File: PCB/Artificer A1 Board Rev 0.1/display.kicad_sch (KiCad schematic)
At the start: 2 parts

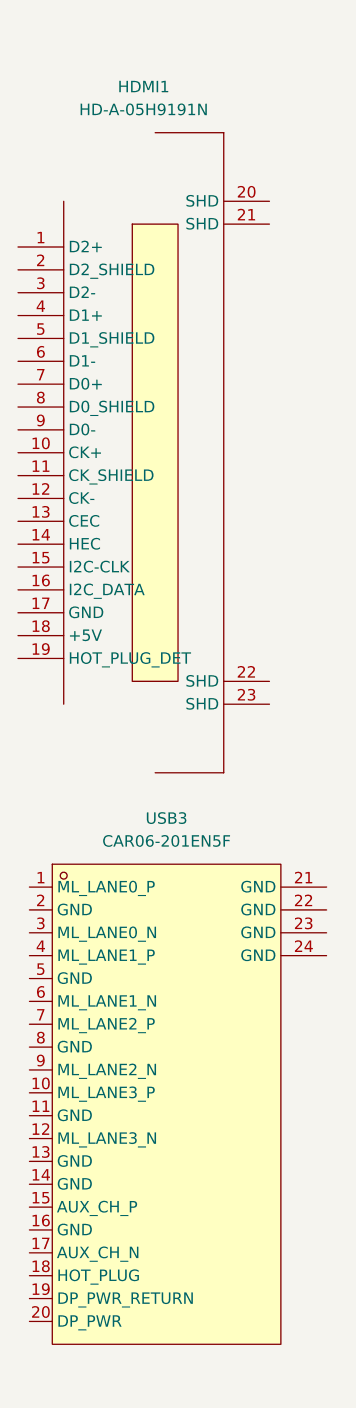
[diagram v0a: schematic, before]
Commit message: localized libraries
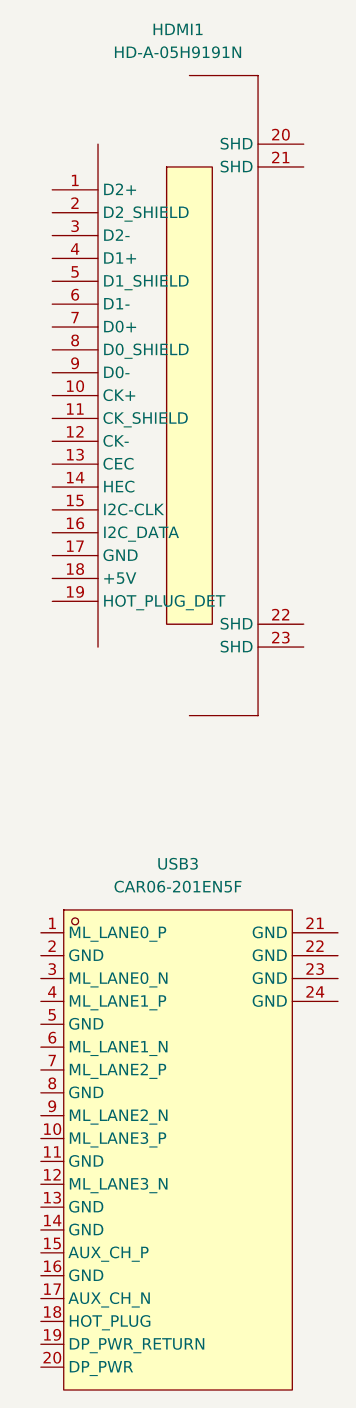
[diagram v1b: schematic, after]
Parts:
- removed HDMI1: HD-A-05H9191N, easyeda2kicad:HDMI-SMD_HD-A-05H9192N, symbol easyeda2kicad:HD-A-05H9191N
- removed USB3: CAR06-201EN5F, easyeda2kicad:DP-SMD_CAR06-201EN5F, symbol easyeda2kicad:CAR06-201EN5F
- added HDMI1: HD-A-05H9191N, easyeda:HDMI-SMD_HD-A-05H9192N, symbol easyeda:HD-A-05H9191N
- added USB3: CAR06-201EN5F, easyeda:DP-SMD_CAR06-201EN5F, symbol easyeda:CAR06-201EN5F
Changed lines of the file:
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@@
 	)
 	(symbol
-		(lib_id "easyeda2kicad:CAR06-201EN5F")
-		(at 142.24 146.05 0)
+		(lib_id "easyeda:CAR06-201EN5F")
+		(at 143.51 151.13 0)
 		(unit 1)
 		(exclude_from_sim no)
@@
 		(fields_autoplaced yes)
 		(property "Reference" "USB3"
-			(at 139.7 113.03 0)
+			(at 140.97 118.11 0)
 			(effects
 				(font
@@
 		)
 		(property "Value" "CAR06-201EN5F"
-			(at 139.7 115.57 0)
-			(effects
-				(font
-					(size 1.27 1.27)
-				)
-			)
-		)
-		(property "Footprint" "easyeda2kicad:DP-SMD_CAR06-201EN5F"
-			(at 142.24 176.53 0)
+			(at 140.97 120.65 0)
+			(effects
+				(font
+					(size 1.27 1.27)
+				)
+			)
+		)
+		(property "Footprint" "easyeda:DP-SMD_CAR06-201EN5F"
+			(at 143.51 181.61 0)
 			(effects
 				(font
@@
 		)
 		(property "Datasheet" ""
-			(at 142.24 146.05 0)
+			(at 143.51 151.13 0)
 			(effects
 				(font
@@
 		)
 		(property "Description" ""
-			(at 142.24 146.05 0)
+			(at 143.51 151.13 0)
 			(effects
 				(font
@@
 		)
 		(property "LCSC Part" "C908454"
-			(at 142.24 179.07 0)
-			(effects
-				(font
-					(size 1.27 1.27)
-				)
-				(hide yes)
-			)
+			(at 143.51 184.15 0)
+			(effects
+				(font
+					(size 1.27 1.27)
+				)
+				(hide yes)
+			)
+		)
+		(pin "19"
+		)
+		(pin "22"
+		)
+		(pin "24"
+		)
+		(pin "11"
+		)
+		(pin "9"
+		)
+		(pin "18"
+		)
+		(pin "5"
+		)
+		(pin "16"
+		)
+		(pin "17"
+		)
+		(pin "8"
 		)
 		(pin "6"
 		)
-		(pin "17"
-		)
-		(pin "19"
-		)
-		(pin "9"
+		(pin "14"
+		)
+		(pin "2"
+		)
+		(pin "1"
+		)
+		(pin "12"
+		)
+		(pin "15"
+		)
+		(pin "3"
+		)
+		(pin "4"
+		)
+		(pin "7"
+		)
+		(pin "10"
+		)
+		(pin "13"
 		)
 		(pin "20"
 		)
-		(pin "14"
-		)
-		(pin "1"
-		)
-		(pin "5"
-		)
-		(pin "10"
-		)
-		(pin "7"
-		)
-		(pin "8"
-		)
-		(pin "11"
-		)
-		(pin "12"
-		)
-		(pin "2"
-		)
-		(pin "15"
-		)
 		(pin "21"
 		)
-		(pin "4"
-		)
-		(pin "16"
-		)
-		(pin "13"
-		)
-		(pin "3"
-		)
-		(pin "18"
-		)
-		(pin "22"
-		)
 		(pin "23"
-		)
-		(pin "24"
 		)
 		(instances
@@
 	)
 	(symbol
-		(lib_id "easyeda2kicad:HD-A-05H9191N")
-		(at 138.43 72.39 0)
+		(lib_id "easyeda:HD-A-05H9191N")
+		(at 142.24 66.04 0)
 		(unit 1)
 		(exclude_from_sim no)
@@
 		(fields_autoplaced yes)
 		(property "Reference" "HDMI1"
-			(at 137.16 31.75 0)
+			(at 140.97 25.4 0)
 			(effects
 				(font
@@
 		)
 		(property "Value" "HD-A-05H9191N"
-			(at 137.16 34.29 0)
-			(effects
-				(font
-					(size 1.27 1.27)
-				)
-			)
-		)
-		(property "Footprint" "easyeda2kicad:HDMI-SMD_HD-A-05H9192N"
-			(at 138.43 107.95 0)
+			(at 140.97 27.94 0)
+			(effects
+				(font
+					(size 1.27 1.27)
+				)
+			)
+		)
+		(property "Footprint" "easyeda:HDMI-SMD_HD-A-05H9192N"
+			(at 142.24 101.6 0)
 			(effects
 				(font
@@
 		)
 		(property "Datasheet" ""
-			(at 138.43 72.39 0)
+			(at 142.24 66.04 0)
 			(effects
 				(font
@@
 		)
 		(property "Description" ""
-			(at 138.43 72.39 0)
+			(at 142.24 66.04 0)
 			(effects
 				(font
@@
 		)
 		(property "LCSC Part" "C18213861"
-			(at 138.43 110.49 0)
-			(effects
-				(font
-					(size 1.27 1.27)
-				)
-				(hide yes)
-			)
+			(at 142.24 104.14 0)
+			(effects
+				(font
+					(size 1.27 1.27)
+				)
+				(hide yes)
+			)
+		)
+		(pin "11"
+		)
+		(pin "7"
+		)
+		(pin "5"
+		)
+		(pin "9"
+		)
+		(pin "10"
+		)
+		(pin "1"
 		)
 		(pin "2"
 		)
-		(pin "1"
+		(pin "6"
+		)
+		(pin "4"
+		)
+		(pin "3"
+		)
+		(pin "8"
+		)
+		(pin "16"
+		)
+		(pin "13"
+		)
+		(pin "15"
+		)
+		(pin "22"
+		)
+		(pin "14"
+		)
+		(pin "12"
+		)
+		(pin "18"
+		)
+		(pin "19"
+		)
+		(pin "23"
+		)
+		(pin "17"
 		)
 		(pin "20"
 		)
-		(pin "12"
-		)
-		(pin "23"
-		)
-		(pin "8"
-		)
-		(pin "9"
-		)
-		(pin "4"
-		)
-		(pin "10"
-		)
-		(pin "11"
-		)
-		(pin "7"
-		)
-		(pin "15"
-		)
-		(pin "16"
-		)
-		(pin "13"
-		)
-		(pin "6"
-		)
-		(pin "14"
-		)
-		(pin "17"
-		)
-		(pin "3"
-		)
-		(pin "5"
-		)
-		(pin "18"
-		)
-		(pin "19"
-		)
 		(pin "21"
 		)
-		(pin "22"
-		)
 		(instances

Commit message: added a few accessories
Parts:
- renumbered USB3 to DP1
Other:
- moved on the sheet: HDMI1
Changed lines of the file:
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@@
 		(dnp no)
 		(fields_autoplaced yes)
-		(property "Reference" "USB3"
+		(property "Reference" "DP1"
 			(at 140.97 118.11 0)
 			(effects
@@
 			(project ""
 				(path "/7c37bdb5-94b0-4567-b5ec-a879db855389/0eff4a68-7f18-47e2-a88b-bcc4ad7e7e86"
-					(reference "USB3")
+					(reference "DP1")
 					(unit 1)
 				)
@@
 	(symbol
 		(lib_id "easyeda:HD-A-05H9191N")
-		(at 142.24 66.04 0)
+		(at 138.43 66.04 0)
 		(unit 1)
 		(exclude_from_sim no)
@@
 		(fields_autoplaced yes)
 		(property "Reference" "HDMI1"
-			(at 140.97 25.4 0)
+			(at 137.16 25.4 0)
 			(effects
 				(font
@@
 		)
 		(property "Value" "HD-A-05H9191N"
-			(at 140.97 27.94 0)
+			(at 137.16 27.94 0)
 			(effects
 				(font
@@
 		)
 		(property "Footprint" "easyeda:HDMI-SMD_HD-A-05H9192N"
-			(at 142.24 101.6 0)
+			(at 138.43 101.6 0)
 			(effects
 				(font
@@
 		)
 		(property "Datasheet" ""
-			(at 142.24 66.04 0)
+			(at 138.43 66.04 0)
 			(effects
 				(font
@@
 		)
 		(property "Description" ""
-			(at 142.24 66.04 0)
+			(at 138.43 66.04 0)
 			(effects
 				(font
@@
 		)
 		(property "LCSC Part" "C18213861"
-			(at 142.24 104.14 0)
+			(at 138.43 104.14 0)
 			(effects
 				(font

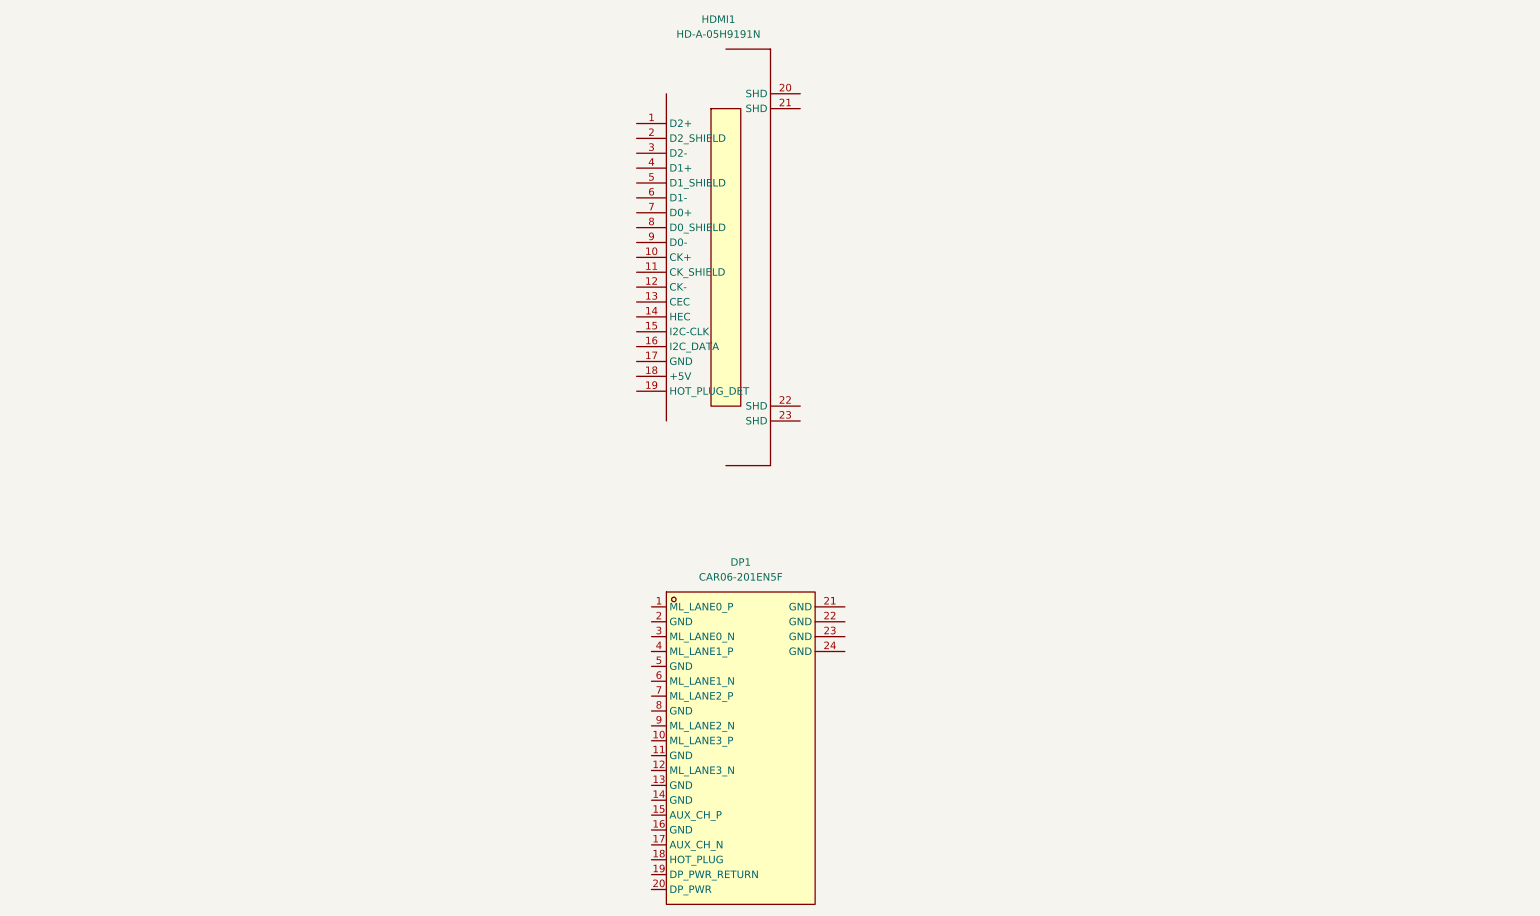
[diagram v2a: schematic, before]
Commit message: added HDMI, DP, DSI, etc
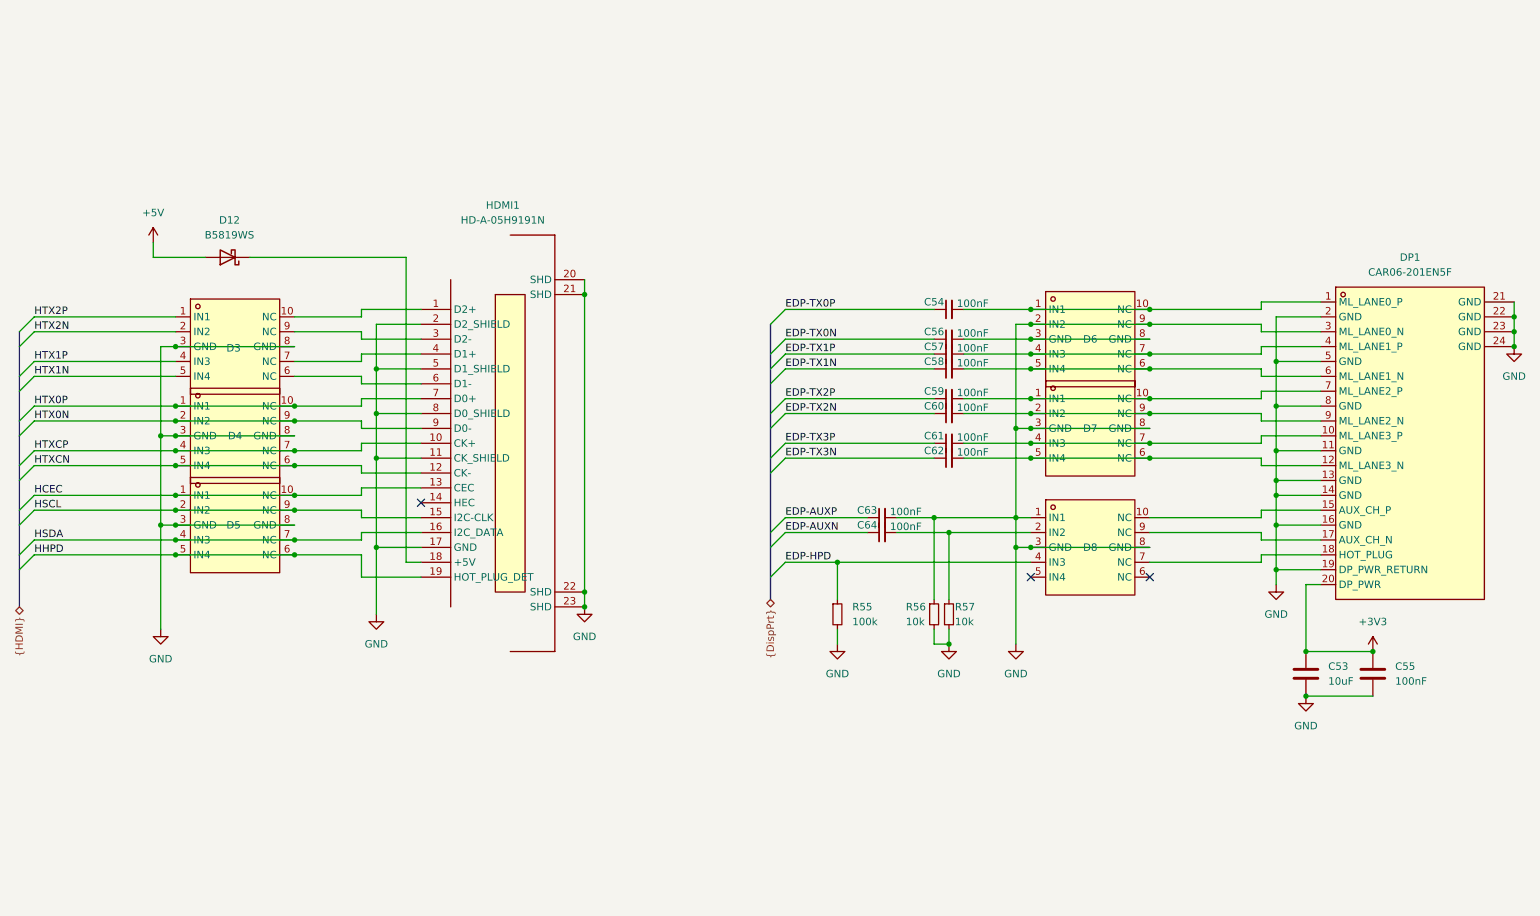
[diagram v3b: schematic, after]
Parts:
- added C53: 10uF, symbol Device:C
- added C54, C56, C57, C58, C59, C60, C61, C62, C63, C64: 100nF, symbol Device:C_Small
- added C55: 100nF, symbol Device:C
- added D12: B5819WS, Diode_SMD:D_SOD-323_HandSoldering, symbol Device:D_Schottky
- added D3, D4, D5, D6, D7, D8: RClamp0524PATCT, easyeda:SLP2510P8_L2.5-W1.0-P0.50-BL, symbol easyeda:RClamp0524PATCT
- added R55: 100k, symbol Device:R_Small
- added R56, R57: 10k, symbol Device:R_Small
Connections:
- net at DP1.1 (ML_LANE0_P): now also C54.2, D6.1 (IN1), D6.10 (NC)
- net at DP1.10 (ML_LANE3_P): now also C61.2, D7.4 (IN3), D7.7 (NC)
- net GND: now reaches DP1.11 (GND)
- net GND: now also DP1.13 (GND), DP1.14 (GND), DP1.16 (GND), DP1.19 (DP_PWR_RETURN), DP1.2 (GND), DP1.21 (GND), DP1.22 (GND), DP1.23 (GND), DP1.24 (GND), DP1.3 (ML_LANE0_N), DP1.5 (GND), DP1.8 (GND), HDMI1.11 (CK_SHIELD), HDMI1.17 (GND), HDMI1.2 (D2_SHIELD), HDMI1.20 (SHD), HDMI1.21 (SHD), HDMI1.22 (SHD), HDMI1.23 (SHD), HDMI1.5 (D1_SHIELD), HDMI1.8 (D0_SHIELD), C53.2, C55.2, C63.2, D3.3 (GND), D3.8 (GND), D4.3 (GND), D4.8 (GND), D5.3 (GND), D5.8 (GND), D6.2 (IN2), D6.9 (NC), D7.3 (GND), D7.8 (GND), D8.1 (IN1), D8.3 (GND), D8.8 (GND), R55.2, R56.1, R56.2, R57.2
- net at DP1.12 (ML_LANE3_N): now also C62.2, D7.5 (IN4), D7.6 (NC)
- net at DP1.15 (AUX_CH_P): now also D8.10 (NC)
- net at DP1.17 (AUX_CH_N): now also D8.9 (NC)
- net at DP1.18 (HOT_PLUG): now also D8.7 (NC)
- net +3V3: now reaches DP1.20 (DP_PWR)
- net +3V3: now also C53.1, C55.1
- net at DP1.4 (ML_LANE1_P): now also C57.2, D6.4 (IN3), D6.7 (NC)
- net at DP1.6 (ML_LANE1_N): now also C58.2, D6.5 (IN4), D6.6 (NC)
- net at DP1.7 (ML_LANE2_P): now also C59.2, D7.1 (IN1), D7.10 (NC)
- net at DP1.9 (ML_LANE2_N): now also C60.2, D7.2 (IN2), D7.9 (NC)
- net at HDMI1.1 (D2+): now also D3.10 (NC)
- net HTXCP: now reaches HDMI1.10 (CK+)
- net HTXCP: now also D4.4 (IN3), D4.7 (NC)
- net HTXCN: now reaches HDMI1.12 (CK-)
- net HTXCN: now also D4.5 (IN4), D4.6 (NC)
- net HCEC: now reaches HDMI1.13 (CEC)
- net HCEC: now also D5.1 (IN1), D5.10 (NC)
- net HSCL: now reaches HDMI1.15 (I2C-CLK)
- net HSCL: now also D5.2 (IN2), D5.9 (NC)
- net HSDA: now reaches HDMI1.16 (I2C_DATA)
- net HSDA: now also D5.4 (IN3), D5.7 (NC)
- net at HDMI1.18 (+5V): now also D12.1 (K)
- net HHPD: now reaches HDMI1.19 (HOT_PLUG_DET)
- net HHPD: now also D5.5 (IN4), D5.6 (NC)
- net at HDMI1.3 (D2-): now also D3.9 (NC)
- net at HDMI1.4 (D1+): now also D3.7 (NC)
- net at HDMI1.6 (D1-): now also D3.6 (NC)
- net HTX0P: now reaches HDMI1.7 (D0+)
- net HTX0P: now also D4.1 (IN1), D4.10 (NC)
- net HTX0N: now reaches HDMI1.9 (D0-)
- net HTX0N: now also D4.2 (IN2), D4.9 (NC)
- new net: C64.2, D8.2 (IN2), R57.1
- new net: C56.2, D6.3 (GND), D6.8 (GND)
- new net +5V: D12.2 (A)
- new net EDP-AUXN: C64.1
- new net EDP-AUXP: C63.1
- new net EDP-HPD: D8.4 (IN3), R55.1
- new net EDP-TX0N: C56.1
- new net EDP-TX0P: C54.1
- new net EDP-TX1N: C58.1
- new net EDP-TX1P: C57.1
- new net EDP-TX2N: C60.1
- new net EDP-TX2P: C59.1
- new net EDP-TX3N: C62.1
- new net EDP-TX3P: C61.1
- new net HTX1N: D3.5 (IN4)
- new net HTX1P: D3.4 (IN3)
- new net HTX2N: D3.2 (IN2)
- new net HTX2P: D3.1 (IN1)
- no-connect marks 0 -> 3
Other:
- moved on the sheet: DP1, HDMI1
